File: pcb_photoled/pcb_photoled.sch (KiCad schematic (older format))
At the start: 4 parts, among them P1 CONN_01X03

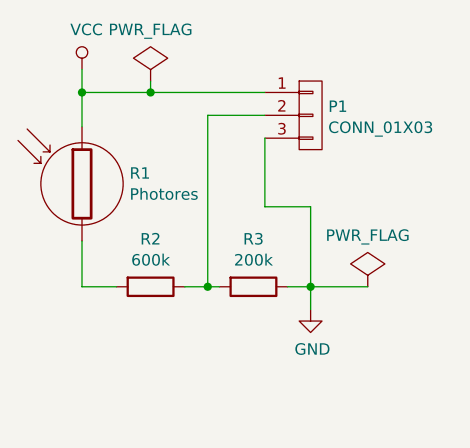
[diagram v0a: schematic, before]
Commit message: Add a capacitor on the adc line, to suppress noise.
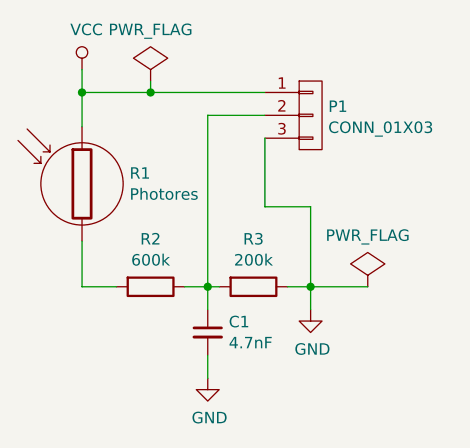
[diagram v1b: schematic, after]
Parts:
- added C1: 4.7nF, Capacitors_SMD:C_0805_HandSoldering, symbol C_Small
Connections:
- net GND: now also C1.2
- net at P1.2 (P2), R2.1, R3.2: now also C1.1
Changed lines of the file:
@@
 LIBS:contrib
 LIBS:valves
+LIBS:pcb_photoled-cache
 EELAYER 25 0
 EELAYER END
@@
 	3550 2450 3300 2450
 Wire Wire Line
-	3300 2450 3300 3200
+	3300 2450 3300 3300
 Connection ~ 3300 3200
 Wire Wire Line
@@
 	1    0    0    -1
 $EndComp
+$Comp
+L C_Small C1
+U 1 1 568801DA
+P 3300 3400
+F 0 "C1" H 3392 3446 50  0000 L CNN
+F 1 "4.7nF" H 3392 3354 50  0000 L CNN
+F 2 "Capacitors_SMD:C_0805_HandSoldering" H 3300 3400 50  0001 C CNN
+F 3 "" H 3300 3400 50  0000 C CNN
+	1    3300 3400
+	1    0    0    -1
+$EndComp
+$Comp
+L GND #PWR05
+U 1 1 5688028F
+P 3300 3600
+F 0 "#PWR05" H 3300 3350 50  0001 C CNN
+F 1 "GND" H 3308 3426 50  0000 C CNN
+F 2 "" H 3300 3600 50  0000 C CNN
+F 3 "" H 3300 3600 50  0000 C CNN
+	1    3300 3600
+	1    0    0    -1
+$EndComp
+Wire Wire Line
+	3300 3600 3300 3500
 $EndSCHEMATC

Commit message: Use a SMD footprint for the BPW photodiode.
This revision was etched and used as v1 PCB for the knpowermeter.
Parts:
- R1: footprint Diodes_ThroughHole:Diode_TO-220_Vertical -> knielsenlib:VBPW34
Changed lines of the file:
@@
 F 0 "R1" H 2958 2796 50  0000 L CNN
 F 1 "Photores" H 2958 2704 50  0000 L CNN
-F 2 "Diodes_ThroughHole:Diode_TO-220_Vertical" V 2680 2750 50  0001 C CNN
+F 2 "knielsenlib:VBPW34" V 2680 2750 50  0001 C CNN
 F 3 "" H 2750 2750 50  0000 C CNN
 	1    2750 2750
